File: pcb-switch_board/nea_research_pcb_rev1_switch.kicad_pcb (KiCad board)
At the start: 4 copper layers, 100 x 39 mm, 8 parts, among them P1 CONN_02X15, P2 CONN_02X13, P3 CONN_02X30, U1 QS4A110, U2 QS4A110, U3 QS4A110, U4 QS4A110, U5 QS4A110

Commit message: -laying out switch board
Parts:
- moved U2 7.11 mm to (-6.69, 2.07)
- moved U3 3.27 mm to (-0.20, 11.7)
- moved U1 2.05 mm to (-17.3, -12.8)
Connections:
- P3 pad 57: GND -> /CTL
- U1 pad 10: /B1_SW -> /MID1_SW
- U1 pad 11: /B1 -> /MID1
- U1 pad 14: /B2 -> /D2
- U1 pad 15: (no net) -> /D2_SW
- U1 pad 16: /C1_SW -> /D1_SW
- U1 pad 17: /C1 -> /D1
- U1 pad 2: /MID1_SW -> /B1_SW
- U1 pad 20: /D1_SW -> /C1_SW
- U1 pad 21: /D1 -> /C1
- U1 pad 22: /D2 -> /B2
- U1 pad 23: /D2_SW -> /B2_SW
- U1 pad 24: Net-(U1-Pad24) -> /5V
- U1 pad 3: /MID1 -> /B1
- U1 pad 4: /MID2 -> /A2
- U1 pad 5: /B2_SW -> /A2_SW
- U1 pad 8: /A2 -> /MID2
- U1 pad 9: /A2_SW -> /MID2_SW
- U2 pad 15: (no net) -> /G2_SW
- U2 pad 24: Net-(U2-Pad24) -> /5V
- U2 pad 5: /G2_SW -> /E2_SW
- U3 pad 15: (no net) -> /L2_SW
- U3 pad 24: Net-(U3-Pad24) -> /5V
- U4 pad 15: (no net) -> /Q2_SW
- U4 pad 24: Net-(U4-Pad24) -> /5V
- U5 pad 15: (no net) -> /V2_SW
- U5 pad 24: Net-(U5-Pad24) -> /5V
- U5 pad 5: /V2_SW -> /T2_SW
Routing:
- net /MID2_SW: track 0.00 -> 34.5 mm
- net /D2_SW: track 0.00 -> 34.1 mm
- net /MID1_SW: track 0.00 -> 33.7 mm
- net /C2_SW: track 0.00 -> 31.7 mm
- net /D1_SW: track 0.00 -> 30.4 mm
- net /A2_SW: track 0.00 -> 28.9 mm
- net /A1_SW: track 0.00 -> 28.2 mm
- net /B2_SW: track 0.00 -> 28.2 mm
- net /C1_SW: track 0.00 -> 27.7 mm
- net /B1_SW: track 0.00 -> 22.6 mm
- net /D1: track 0.00 -> 21.2 mm, vias 0 -> 1
- net /B1: track 0.00 -> 20.7 mm, vias 0 -> 2
- net /C1: track 0.00 -> 20.3 mm, vias 0 -> 1
- net /MID1: track 0.00 -> 18.0 mm, vias 0 -> 1
- net /D2: track 0.00 -> 15.5 mm, vias 0 -> 1
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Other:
- board size 100 x 39 mm -> 100 x 50 mm
- copper layers 4 -> 2
- net class Default: clearance 0.2 -> 0.1524; trace_width 0.25 -> 0.1524
- rule trace_clearance: 0.2 -> 0.1524

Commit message: -progress on switch board layout
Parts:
- moved U5 12.5 mm to (11.0, 7.63)
- moved U2 10.3 mm to (-17.0, 2.45)
- moved U4 9.27 mm to (7.07, -5.35)
- moved U3 2.79 mm to (-2.74, 10.5)
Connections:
- U2 pad 10: /G1_SW -> /E1_SW
- U2 pad 11: /G1 -> /E1
- U2 pad 14: /G2 -> /I2
- U2 pad 15: /G2_SW -> /I2_SW
- U2 pad 16: /H1_SW -> /I1_SW
- U2 pad 17: /H1 -> /I1
- U2 pad 2: /E1_SW -> /G1_SW
- U2 pad 20: /I1_SW -> /H1_SW
- U2 pad 21: /I1 -> /H1
- U2 pad 22: /I2 -> /G2
- U2 pad 23: /I2_SW -> /G2_SW
- U2 pad 3: /E1 -> /G1
- U2 pad 4: /E2 -> /F2
- U2 pad 5: /E2_SW -> /F2_SW
- U2 pad 8: /F2 -> /E2
- U2 pad 9: /F2_SW -> /E2_SW
- U3 pad 10: /L1_SW -> /J1_SW
- U3 pad 11: /L1 -> /J1
- U3 pad 2: /J1_SW -> /L1_SW
- U3 pad 3: /J1 -> /L1
- U3 pad 4: /J2 -> /K2
- U3 pad 5: /J2_SW -> /K2_SW
- U3 pad 8: /K2 -> /J2
- U3 pad 9: /K2_SW -> /J2_SW
- U4 pad 10: /Q1_SW -> /O1_SW
- U4 pad 11: /Q1 -> /O1
- U4 pad 2: /O1_SW -> /Q1_SW
- U4 pad 3: /O1 -> /Q1
- U4 pad 4: /O2 -> /P2
- U4 pad 5: /O2_SW -> /P2_SW
- U4 pad 8: /P2 -> /O2
- U4 pad 9: /P2_SW -> /O2_SW
- U5 pad 14: /V2 -> /SCL
- U5 pad 15: /V2_SW -> /SCL_SW
- U5 pad 16: /LED1_SW -> /SDA_SW
- U5 pad 17: /LED1 -> /SDA
- U5 pad 20: /SDA_SW -> /LED1_SW
- U5 pad 21: /SDA -> /LED1
- U5 pad 22: /SCL -> /V2
- U5 pad 23: /SCL_SW -> /V2_SW
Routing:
- net /CTL: track 0.84 -> 188.8 mm, vias 1 -> 6
- net GND: track 0.71 -> 154.6 mm, vias 1 -> 5
- net /5V: track 0.00 -> 135.2 mm, vias 0 -> 1
- net /L2: track 0.00 -> 65.9 mm, vias 0 -> 1
- net /M1: track 0.00 -> 59.5 mm, vias 0 -> 1
- net /M2: track 0.00 -> 57.5 mm, vias 0 -> 1
- net /L1: track 0.00 -> 54.3 mm, vias 0 -> 1
- net /L2_SW: track 0.00 -> 53.0 mm, vias 0 -> 1
- net /N1: track 0.00 -> 51.8 mm, vias 0 -> 1
- net /N2: track 0.00 -> 51.1 mm, vias 0 -> 1
- net /MID2: track 1.50 -> 52.4 mm
- net /3V3: track 0.00 -> 50.2 mm
- net /M2_SW: track 0.00 -> 48.9 mm, vias 0 -> 1
- net /J2_SW: track 0.00 -> 47.2 mm, vias 0 -> 1
- net /M1_SW: track 0.00 -> 47.1 mm, vias 0 -> 1
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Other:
- copper layers 2 -> 4

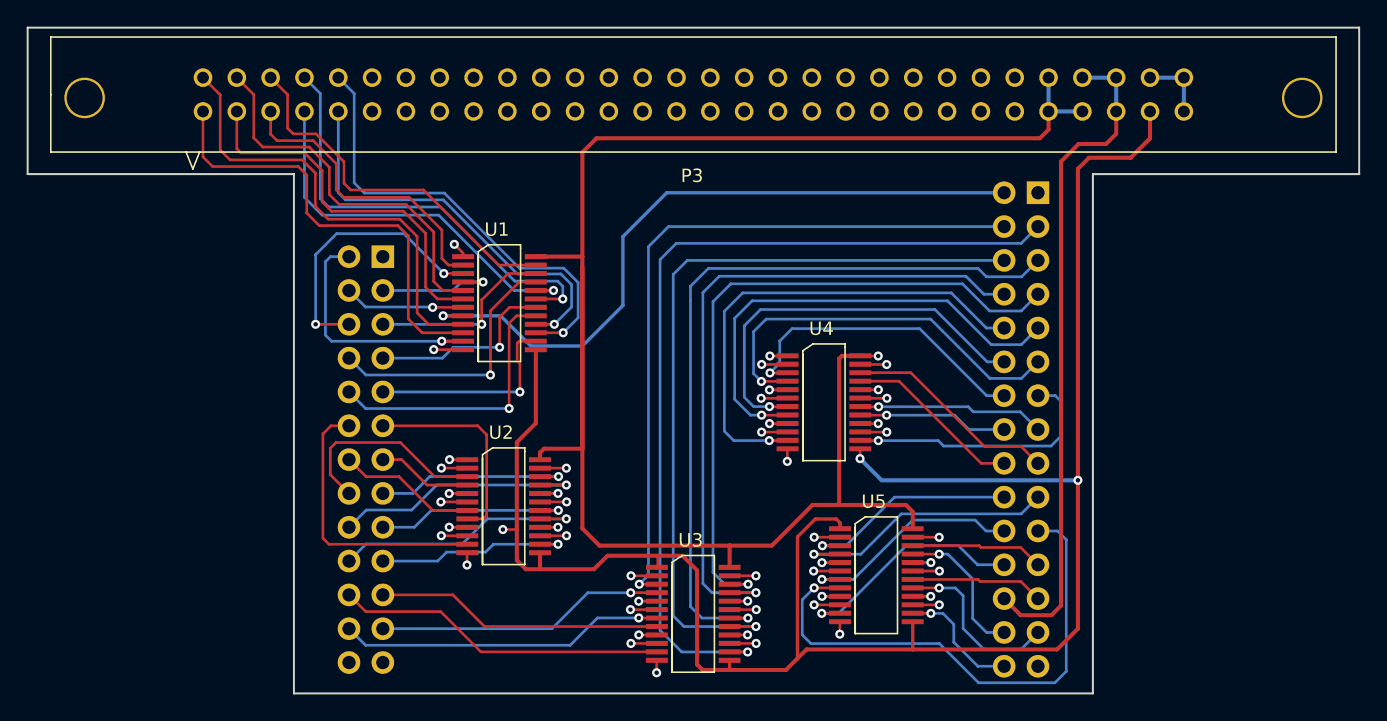
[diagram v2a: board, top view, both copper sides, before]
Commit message: -finished rev1 of switch board layout -zip file sent off for pcb order
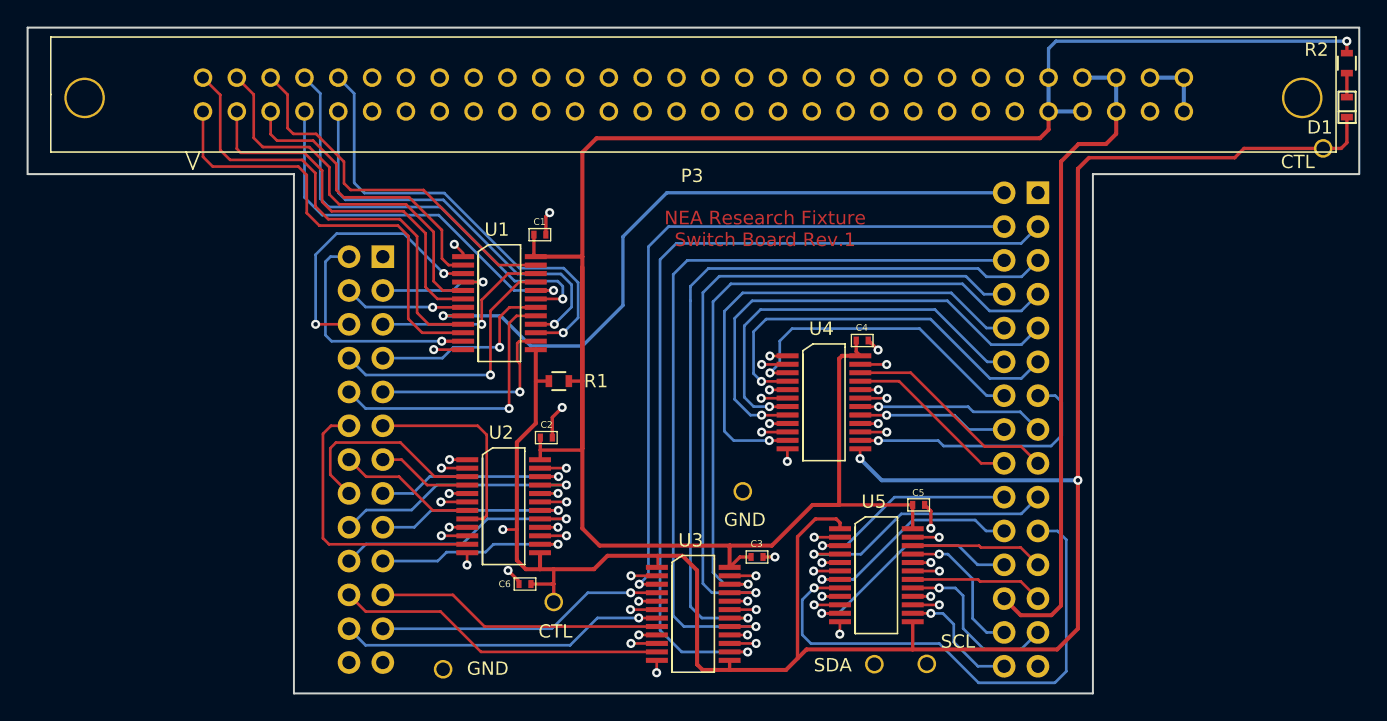
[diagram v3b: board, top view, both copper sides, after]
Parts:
- added C1: 0.1uF, footprints_on_Cdrive:0402, F.Cu at (-11.5, -14.5)
- added C2: 0.1uF, footprints_on_Cdrive:0402, F.Cu at (-11.0, 0.79)
- added C3: 0.1uF, footprints_on_Cdrive:0402, F.Cu at (4.78, 9.75)
- added C4: 0.1uF, footprints_on_Cdrive:0402, F.Cu at (12.7, -6.50)
- added C5: 0.1uF, footprints_on_Cdrive:0402, F.Cu at (16.9, 5.84)
- added C6: 0.1uF, footprints_on_Cdrive:0402, F.Cu at (-12.6, 11.8)
- added D1: LED_SMT, footprints:0603-D, F.Cu at (49.1, -24.0)
- added R1: 10k, footprints_on_Cdrive:0603, F.Cu at (-10.1, -3.45)
- added R2: 75, footprints_on_Cdrive:0603, F.Cu at (49.1, -27.3)
- added TP1: header_pin, footprints_on_Cdrive:Header_Pin_Rnd, F.Cu at (3.71, 4.83)
- added TP2: header_pin, footprints_on_Cdrive:Header_Pin_Rnd, F.Cu at (-18.8, 18.2)
- added TP3: header_pin, footprints_on_Cdrive:Header_Pin_Rnd, F.Cu at (-10.5, 13.1)
- added TP4: header_pin, footprints_on_Cdrive:Header_Pin_Rnd, F.Cu at (47.3, -20.9)
- added TP7: header_pin, footprints_on_Cdrive:Header_Pin_Rnd, F.Cu at (17.5, 17.8)
- added TP8: header_pin, footprints_on_Cdrive:Header_Pin_Rnd, F.Cu at (13.6, 17.8)
- P1: footprint Pin_Header_Straight_2x15_Pitch2.54mm -> footprints_on_Cdrive:Pin_Header_Straight_2x15_Pitch2.54mm
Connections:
- P3 pad 57: /CTL -> Net-(P3-Pad57)
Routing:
- net /5V: track 135.2 -> 166.8 mm
- net /CTL: track 188.8 -> 208.7 mm
- net GND: track 154.6 -> 164.2 mm, vias 5 -> 11
- net /SDA_SW: track 41.0 -> 48.8 mm
- net /SCL_SW: track 45.7 -> 50.5 mm
- net Net-(D1-Pad1): track 0.00 -> 1.80 mm
- added copper zone on In2.Cu, net GND
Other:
- board text added: "CTL"
- board text added: "GND"
- board text added: "NEA Research Fixture Switch Board Rev.1"
- board text added: "SCL"
- board text added: "SDA"
